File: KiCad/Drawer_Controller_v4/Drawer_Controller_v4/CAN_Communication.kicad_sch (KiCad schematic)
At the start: 13 parts, among them Q37 AO3400A, U8 SN65HVD230

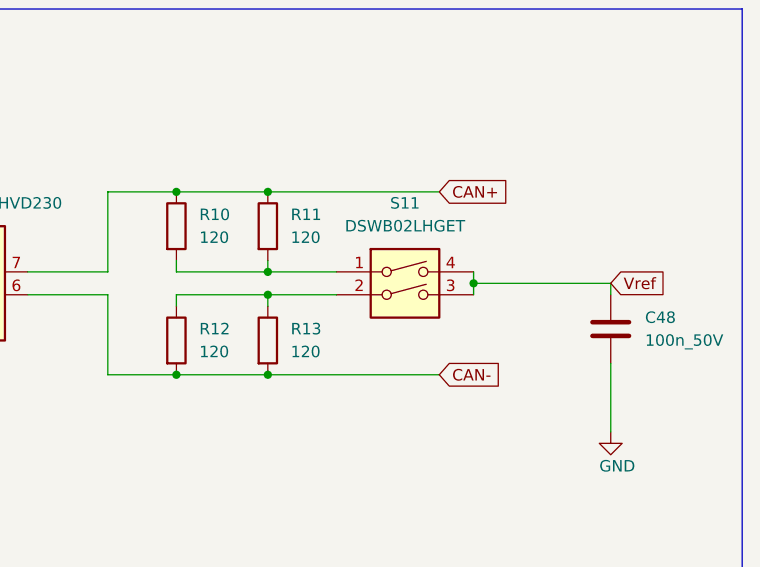
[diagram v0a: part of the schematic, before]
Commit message: feat: placed all parts for `Drawer_Controller_v4` and routed about 80%
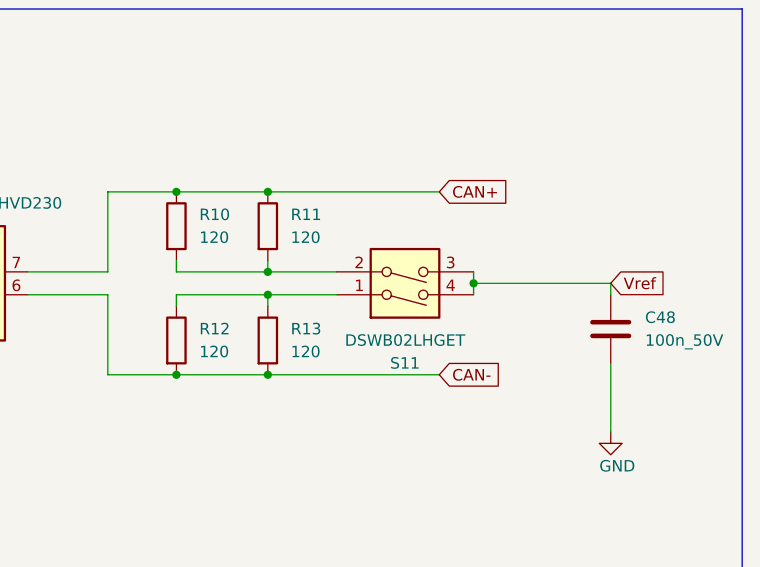
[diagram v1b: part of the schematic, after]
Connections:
- net at R12.1, R13.1: now also S11.1; no longer S11.2
- net at R10.2, R11.2: now also S11.2; no longer S11.1
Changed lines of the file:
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@@
 	(symbol
 		(lib_id "_Switch:DSWB02LHGET")
-		(at 203.2 110.49 0)
+		(at 203.2 107.95 0)
+		(mirror x)
 		(unit 1)
 		(exclude_from_sim no)
@@
 		(on_board yes)
 		(dnp no)
-		(fields_autoplaced yes)
 		(property "Reference" "S11"
-			(at 203.2 100.33 0)
+			(at 203.2 118.11 0)
 			(effects
 				(font
@@
 		)
 		(property "Value" "DSWB02LHGET"
-			(at 203.2 102.87 0)
+			(at 203.2 115.57 0)
 			(effects
 				(font
@@
 		)
 		(property "Footprint" "Robast:DSWB02LHGET"
-			(at 203.2 110.49 0)
+			(at 203.2 107.95 0)
 			(effects
 				(font
@@
 		)
 		(property "Datasheet" "https://datasheet.lcsc.com/lcsc/2309061745_DongGuan-KINGTEK-Industrial-Co--LTD-DSWB02LHGET_C99421.pdf"
-			(at 203.2 110.49 0)
+			(at 203.2 107.95 0)
 			(effects
 				(font
@@
 		)
 		(property "Description" "2Bit SPST Red Slide"
-			(at 203.2 110.49 0)
+			(at 203.2 107.95 0)
 			(effects
 				(font
@@
 		)
 		(property "MF" "DongGuan KINGTEK Industrial Co.,LTD"
-			(at 203.2 110.49 0)
+			(at 203.2 107.95 0)
 			(effects
 				(font
@@
 		)
 		(property "MPN" "DSWB02LHGET"
-			(at 203.2 110.49 0)
+			(at 203.2 107.95 0)
 			(effects
 				(font
@@
 		)
 		(property "OC_LCSC" "C99421"
-			(at 203.2 110.49 0)
+			(at 203.2 107.95 0)
 			(effects
 				(font
@@
 		)
 		(property "OC_MOUSER" ""
-			(at 203.2 110.49 0)
+			(at 203.2 107.95 0)
 			(effects
 				(font

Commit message: feat: completed `Drawer_Controller_v4`
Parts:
- renumbered C7 to C14, C19 to C15, C48 to C16, Q37 to Q1, R9 to R10, R5 to R11, R10 to R12, R12 to R13, R11 to R14, R13 to R15, R8 to R9, S11 to S1, U8 to U4
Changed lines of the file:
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@@
 		(dnp no)
 		(fields_autoplaced yes)
-		(property "Reference" "C19"
+		(property "Reference" "C15"
 			(at 137.16 90.1699 0)
 			(effects
@@
 			(project "Drawer_Controller_v4"
 				(path "/57f8c193-fe09-43d3-9441-dbd40881d2aa/1e314787-7f45-4847-9ba5-2ff173980b3b"
-					(reference "C19")
+					(reference "C15")
 					(unit 1)
 				)
@@
 		(dnp no)
 		(fields_autoplaced yes)
-		(property "Reference" "R9"
+		(property "Reference" "R10"
 			(at 102.87 121.9199 0)
 			(effects
@@
 			(project "Drawer_Controller_v4"
 				(path "/57f8c193-fe09-43d3-9441-dbd40881d2aa/1e314787-7f45-4847-9ba5-2ff173980b3b"
-					(reference "R9")
+					(reference "R10")
 					(unit 1)
 				)
@@
 		(dnp no)
 		(fields_autoplaced yes)
-		(property "Reference" "R13"
+		(property "Reference" "R15"
 			(at 190.5 114.2999 0)
 			(effects
@@
 			(project "Drawer_Controller_v4"
 				(path "/57f8c193-fe09-43d3-9441-dbd40881d2aa/1e314787-7f45-4847-9ba5-2ff173980b3b"
-					(reference "R13")
+					(reference "R15")
 					(unit 1)
 				)
@@
 		(on_board yes)
 		(dnp no)
-		(property "Reference" "S11"
+		(property "Reference" "S1"
 			(at 203.2 118.11 0)
 			(effects
@@
 			(project "Drawer_Controller_v4"
 				(path "/57f8c193-fe09-43d3-9441-dbd40881d2aa/1e314787-7f45-4847-9ba5-2ff173980b3b"
-					(reference "S11")
+					(reference "S1")
 					(unit 1)
 				)
@@
 		(dnp no)
 		(fields_autoplaced yes)
-		(property "Reference" "C48"
+		(property "Reference" "C16"
 			(at 229.87 113.0299 0)
 			(effects
@@
 			(project "Drawer_Controller_v4"
 				(path "/57f8c193-fe09-43d3-9441-dbd40881d2aa/1e314787-7f45-4847-9ba5-2ff173980b3b"
-					(reference "C48")
+					(reference "C16")
 					(unit 1)
 				)
@@
 		(on_board yes)
 		(dnp no)
-		(property "Reference" "#PWR0163"
+		(property "Reference" "#PWR058"
 			(at 111.76 133.35 0)
 			(effects
@@
 			(project "Drawer_Controller_v4"
 				(path "/57f8c193-fe09-43d3-9441-dbd40881d2aa/1e314787-7f45-4847-9ba5-2ff173980b3b"
-					(reference "#PWR0163")
+					(reference "#PWR058")
 					(unit 1)
 				)
@@
 		(on_board yes)
 		(dnp no)
-		(property "Reference" "#PWR050"
+		(property "Reference" "#PWR060"
 			(at 115.57 101.6 0)
 			(effects
@@
 			(project "Drawer_Controller_v4"
 				(path "/57f8c193-fe09-43d3-9441-dbd40881d2aa/1e314787-7f45-4847-9ba5-2ff173980b3b"
-					(reference "#PWR050")
+					(reference "#PWR060")
 					(unit 1)
 				)
@@
 		(dnp no)
 		(fields_autoplaced yes)
-		(property "Reference" "C7"
+		(property "Reference" "C14"
 			(at 119.38 90.1699 0)
 			(effects
@@
 			(project "Drawer_Controller_v4"
 				(path "/57f8c193-fe09-43d3-9441-dbd40881d2aa/1e314787-7f45-4847-9ba5-2ff173980b3b"
-					(reference "C7")
+					(reference "C14")
 					(unit 1)
 				)
@@
 		(dnp no)
 		(fields_autoplaced yes)
-		(property "Reference" "#PWR044"
+		(property "Reference" "#PWR059"
 			(at 115.57 88.9 0)
 			(effects
@@
 			(project "Drawer_Controller_v4"
 				(path "/57f8c193-fe09-43d3-9441-dbd40881d2aa/1e314787-7f45-4847-9ba5-2ff173980b3b"
-					(reference "#PWR044")
+					(reference "#PWR059")
 					(unit 1)
 				)
@@
 		(on_board yes)
 		(dnp no)
-		(property "Reference" "#PWR036"
+		(property "Reference" "#PWR062"
 			(at 133.35 133.35 0)
 			(effects
@@
 			(project "Drawer_Controller_v4"
 				(path "/57f8c193-fe09-43d3-9441-dbd40881d2aa/1e314787-7f45-4847-9ba5-2ff173980b3b"
-					(reference "#PWR036")
+					(reference "#PWR062")
 					(unit 1)
 				)
@@
 		(on_board yes)
 		(dnp no)
-		(property "Reference" "#PWR04"
+		(property "Reference" "#PWR064"
 			(at 226.06 132.08 0)
 			(effects
@@
 			(project "Drawer_Controller_v4"
 				(path "/57f8c193-fe09-43d3-9441-dbd40881d2aa/1e314787-7f45-4847-9ba5-2ff173980b3b"
-					(reference "#PWR04")
+					(reference "#PWR064")
 					(unit 1)
 				)
@@
 		(dnp no)
 		(fields_autoplaced yes)
-		(property "Reference" "R12"
+		(property "Reference" "R13"
 			(at 180.34 114.2999 0)
 			(effects
@@
 			(project "Drawer_Controller_v4"
 				(path "/57f8c193-fe09-43d3-9441-dbd40881d2aa/1e314787-7f45-4847-9ba5-2ff173980b3b"
-					(reference "R12")
+					(reference "R13")
 					(unit 1)
 				)
@@
 		(on_board yes)
 		(dnp no)
-		(property "Reference" "#PWR038"
+		(property "Reference" "#PWR061"
 			(at 133.35 101.6 0)
 			(effects
@@
 			(project "Drawer_Controller_v4"
 				(path "/57f8c193-fe09-43d3-9441-dbd40881d2aa/1e314787-7f45-4847-9ba5-2ff173980b3b"
-					(reference "#PWR038")
+					(reference "#PWR061")
 					(unit 1)
 				)
@@
 		(dnp no)
 		(fields_autoplaced yes)
-		(property "Reference" "R10"
+		(property "Reference" "R12"
 			(at 180.34 101.5999 0)
 			(effects
@@
 			(project "Drawer_Controller_v4"
 				(path "/57f8c193-fe09-43d3-9441-dbd40881d2aa/1e314787-7f45-4847-9ba5-2ff173980b3b"
-					(reference "R10")
+					(reference "R12")
 					(unit 1)
 				)
@@
 		(dnp no)
 		(fields_autoplaced yes)
-		(property "Reference" "U8"
+		(property "Reference" "U4"
 			(at 153.3241 97.79 0)
 			(effects
@@
 			(project "Drawer_Controller_v4"
 				(path "/57f8c193-fe09-43d3-9441-dbd40881d2aa/1e314787-7f45-4847-9ba5-2ff173980b3b"
-					(reference "U8")
+					(reference "U4")
 					(unit 1)
 				)
@@
 		(dnp no)
 		(fields_autoplaced yes)
-		(property "Reference" "#PWR035"
+		(property "Reference" "#PWR056"
 			(at 52.07 29.21 0)
 			(effects
@@
 			(project "Drawer_Controller_v4"
 				(path "/57f8c193-fe09-43d3-9441-dbd40881d2aa/1e314787-7f45-4847-9ba5-2ff173980b3b"
-					(reference "#PWR035")
+					(reference "#PWR056")
 					(unit 1)
 				)
@@
 		(on_board yes)
 		(dnp no)
-		(property "Reference" "#PWR052"
+		(property "Reference" "#PWR063"
 			(at 151.13 133.35 0)
 			(effects
@@
 			(project "Drawer_Controller_v4"
 				(path "/57f8c193-fe09-43d3-9441-dbd40881d2aa/1e314787-7f45-4847-9ba5-2ff173980b3b"
-					(reference "#PWR052")
+					(reference "#PWR063")
 					(unit 1)
 				)
@@
 		(dnp no)
 		(fields_autoplaced yes)
-		(property "Reference" "R11"
+		(property "Reference" "R14"
 			(at 190.5 101.5999 0)
 			(effects
@@
 			(project "Drawer_Controller_v4"
 				(path "/57f8c193-fe09-43d3-9441-dbd40881d2aa/1e314787-7f45-4847-9ba5-2ff173980b3b"
-					(reference "R11")
+					(reference "R14")
 					(unit 1)
 				)
@@
 		(on_board yes)
 		(dnp no)
-		(property "Reference" "#PWR037"
+		(property "Reference" "#PWR057"
 			(at 62.23 36.195 0)
 			(effects
@@
 			(project "Drawer_Controller_v4"
 				(path "/57f8c193-fe09-43d3-9441-dbd40881d2aa/1e314787-7f45-4847-9ba5-2ff173980b3b"
-					(reference "#PWR037")
+					(reference "#PWR057")
 					(unit 1)
 				)
@@
 		(dnp no)
 		(fields_autoplaced yes)
-		(property "Reference" "Q37"
+		(property "Reference" "Q1"
 			(at 115.57 116.8399 0)
 			(effects
@@
 			(project "Drawer_Controller_v4"
 				(path "/57f8c193-fe09-43d3-9441-dbd40881d2aa/1e314787-7f45-4847-9ba5-2ff173980b3b"
-					(reference "Q37")
+					(reference "Q1")
 					(unit 1)
 				)
@@
 		(dnp no)
 		(fields_autoplaced yes)
-		(property "Reference" "R5"
+		(property "Reference" "R11"
 			(at 130.81 116.8399 0)
 			(effects
@@
 			(project "Drawer_Controller_v4"
 				(path "/57f8c193-fe09-43d3-9441-dbd40881d2aa/1e314787-7f45-4847-9ba5-2ff173980b3b"
-					(reference "R5")
+					(reference "R11")
 					(unit 1)
 				)
@@
 		(dnp no)
 		(fields_autoplaced yes)
-		(property "Reference" "R8"
+		(property "Reference" "R9"
 			(at 91.44 111.76 90)
 			(effects
@@
 			(project "Drawer_Controller_v4"
 				(path "/57f8c193-fe09-43d3-9441-dbd40881d2aa/1e314787-7f45-4847-9ba5-2ff173980b3b"
-					(reference "R8")
-					(unit 1)
-				)
+					(reference "R9")
+					(unit 1)
+				)
